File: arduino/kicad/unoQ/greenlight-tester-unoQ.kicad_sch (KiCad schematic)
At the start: 44 parts, among them J1 AudioJack2, J1 Conn_01x08, J2 AudioJack2, J2 Conn_01x10, J3 Conn_01x06, J3 XLR3, J4 XLR3, J6 Conn_01x08, K1 Relay_DPDT, K2 Relay_DPDT, K3 Relay_DPDT, K4 Relay_DPDT, K5 Relay_DPDT, K6 Relay_DPDT, Q1 PN2222A, Q2 PN2222A, Q3 PN2222A, Q4 PN2222A, Q5 PN2222A, Q6 PN2222A

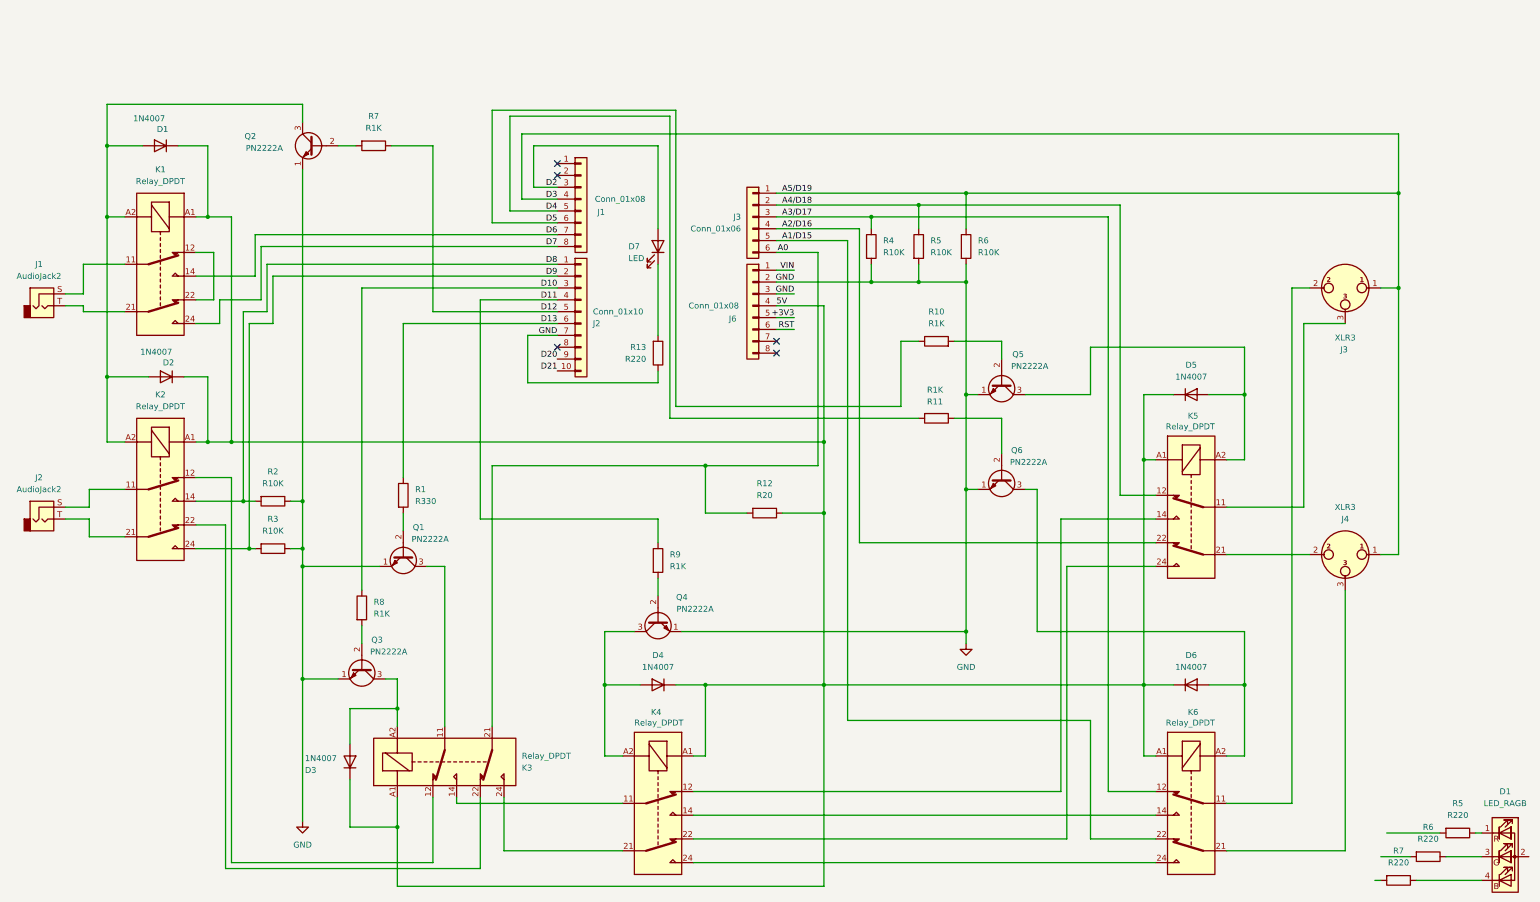
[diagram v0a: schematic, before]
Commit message: UNO Q tester: reconcile sketch with as-built schematic
The stacked proto boards ran short of through-holes, so pins were
reassigned. The schematic now matches the board and is the source of truth.

Schematic: re-annotated (headers are H*, jacks are J*), XLR pin 1 split
(D4 drives J4, A5 senses J3), K5/K6 each switch one conductor at both ends
so XRES can close a loop, R8 sense resistor fed from +3V3 (A0 is not 5V
tolerant), Q4 gets a base resistor, and the result LED anode goes to +3V3.

Sketch:
- K3 D4 -> D5, K4 D5 -> D12, XLR pin 1 drive D12 -> D4
- XLR sense: pin 2 = A4, pin 3 = A3, matching the relay that carries each pin
- D20/D21 now drive the red/green result LED (active-low)
- XSHELL returns ERROR:NOT_SUPPORTED:XSHELL; the shell has no wiring left

arduino/CLAUDE.md pin section rewritten (it described an older layout).

Co-Authored-By: Claude Opus 5.5 <noreply@anthropic.com>
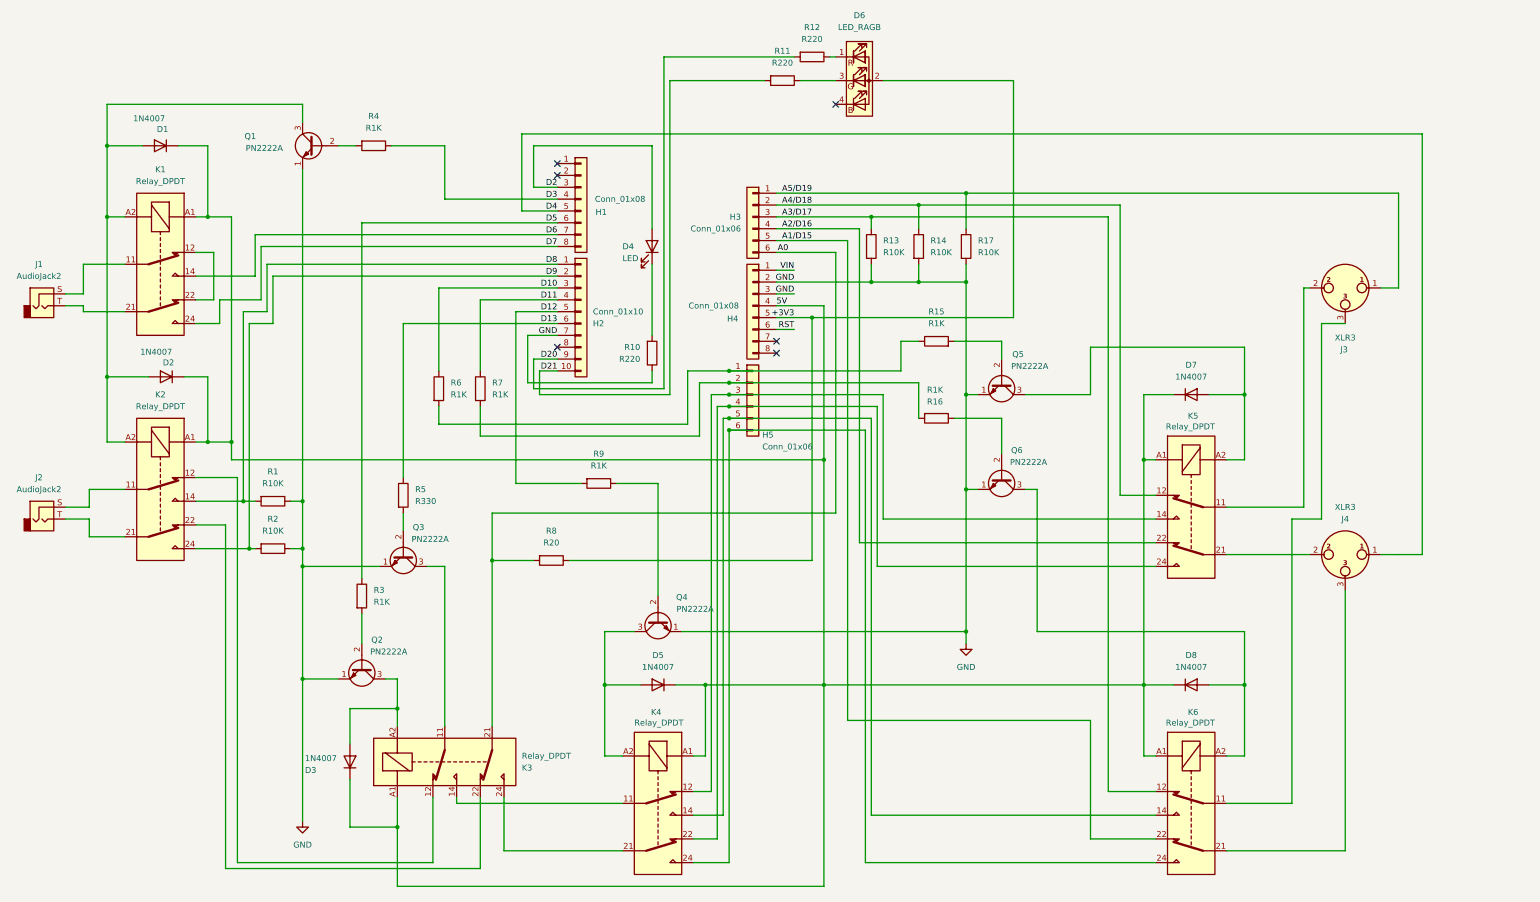
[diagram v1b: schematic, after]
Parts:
- removed R7: R220, Resistor_THT:R_Axial_DIN0204_L3.6mm_D1.6mm_P1.90mm_Vertical, symbol Device:R
- added H5: Conn_01x06, symbol Connector_Generic:Conn_01x06
- added R3, R9: R1K, Resistor_THT:R_Axial_DIN0204_L3.6mm_D1.6mm_P1.90mm_Vertical, symbol Device:R
- renumbered D7 to D4, D4 to D5, D1 to D6, D5 to D7, D6 to D8, J1 to H1, J2 to H2, J3 to H3, J6 to H4, Q2 to Q1, Q3 to Q2, Q1 to Q3, R2 to R1, R13 to R10, R6 to R11, R5 to R12, R4 to R13, R5 to R14, R10 to R15, R11 to R16, R6 to R17, R3 to R2, R7 to R4, R1 to R5, R8 to R6, R9 to R7, R12 to R8
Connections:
- net +3V3: now also D6.2 (A), R8.1
- net 5V: no longer R8.1
- net A5/D19: no longer H1.4 (D3), J4.1
- net D12: now also R9.2; no longer R4.1
- net D20: now also R12.2
- net D21: now also R11.2
- net D4: now also J4.1; no longer R16.2
- net D5: now also R3.1; no longer R15.1
- net at R7.2: now also R16.2, H5.2 (Pin_2); no longer Q4.2 (B)
- net at K4.12, K5.14: now also H5.3 (Pin_3)
- net at K4.14, K6.14: now also H5.5 (Pin_5)
- net at K4.22, K5.24: now also H5.4 (Pin_4)
- net at K4.24, K6.24: now also H5.6 (Pin_6)
- net at J3.2: now also K5.11; no longer K6.11
- net at J3.3: now also K6.11; no longer K5.11
- net at R6.2: now also R15.1, H5.1 (Pin_1); no longer Q2.2 (B)
- new net: Q4.2 (B), R9.1
- new net: Q2.2 (B), R3.2
- new net D3: H1.4 (D3), R4.1
- no-connect marks 5 -> 6
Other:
- moved on the sheet: D4, D6, R10, R11, R12, R6, R7, R8
